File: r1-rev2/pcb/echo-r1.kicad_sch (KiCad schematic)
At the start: 74 parts, among them J2 TYPE-C-31-M-12, J3 TF-115, J6 PM254-1-06-W-8.5, J7 ILI9342C, Q4 AO3401A, SW1 POWER, SW10 DPAD→, SW11 START, SW12 SELECT, SW13 VOL+, SW14 VOL-, SW2 HOLD, SW3 A, SW4 B, SW5 X, SW6 Y, SW7 DPAD↑, SW8 DPAD↓, SW9 DPAD←, U7 STM32H7R3Z8Jx, U8 W958D8NBYA5I, Y1 SC-32S32.768kHz20PPM12.5pF, Y2 XTM32024000JT00351001

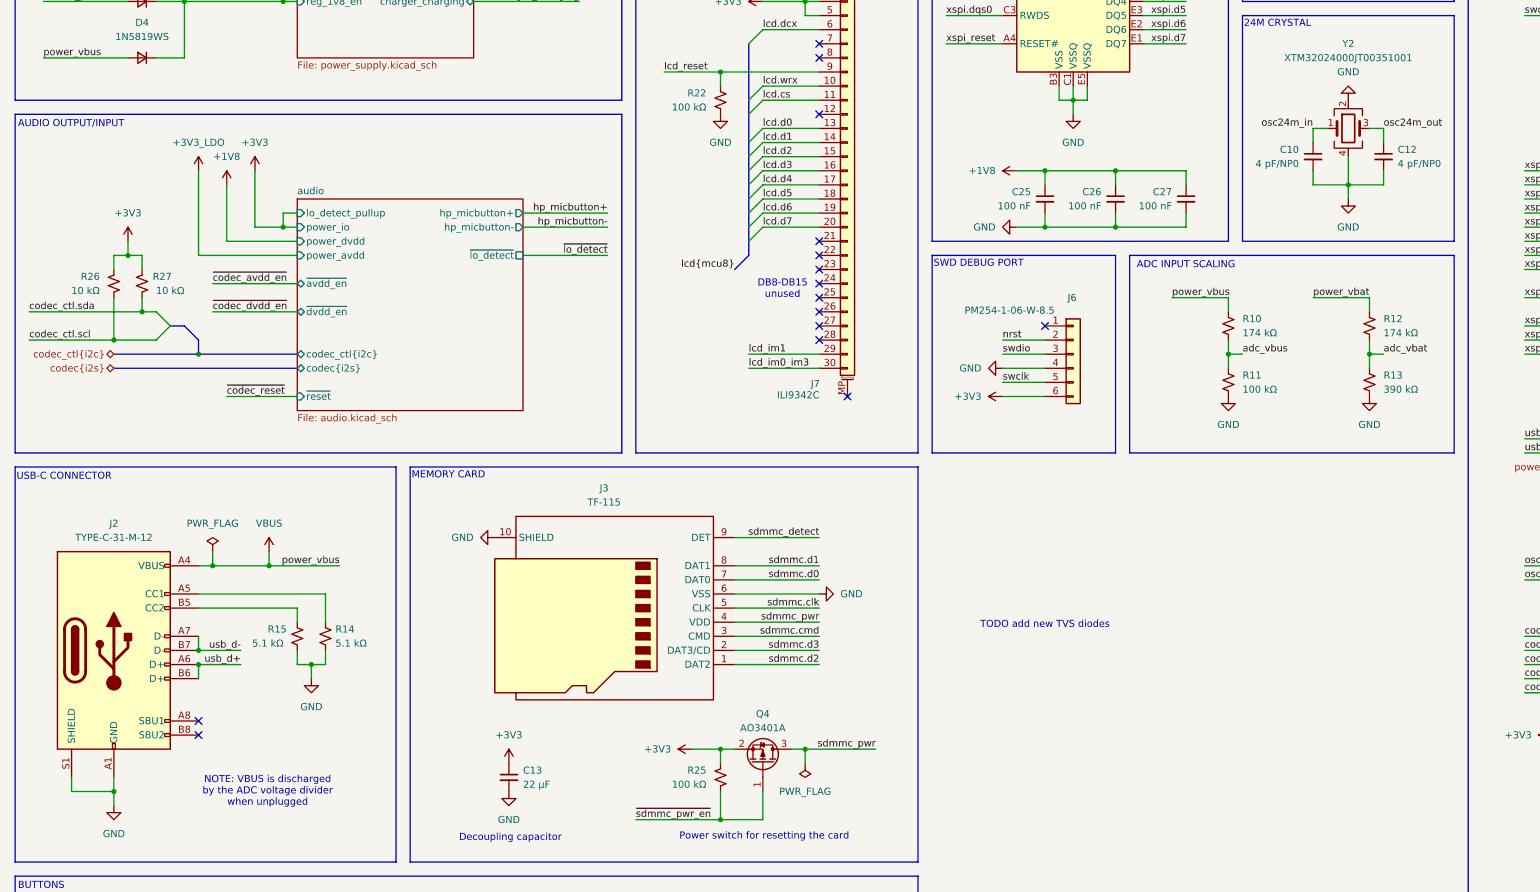
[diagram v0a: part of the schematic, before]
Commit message: R1-Rev2: optimize resistor values
- Resistors used for the ADC dividers were way too high; I didn't
  take into account how the RC constant affected ADC performance
  so the conversion accuracy was probably poor. The new values are
  based on ST's recommendations and the theoretical resolution is
  computed in a spreadsheet.
- Simplify LO detect, originally I had the idea of a "wake on jack
  insert" feature but this is not possible for the headphone jack
  because it is only polled over I2C. The reason for the big 1M
  resistor that was there in Rev1 was to keep the effect on ground
  minimal. If the MCU is powered up then a simple hi-z input with
  internal pullup does the job better.
- Standardize on just 4 unique resistor values to reduce the cost
  of assembly: 5.1k is needed for USB, 2.2k for micbias and battery
  charge reference, and 15k and 68k for voltage reference. Other
  resistors have been rounded to one of these.
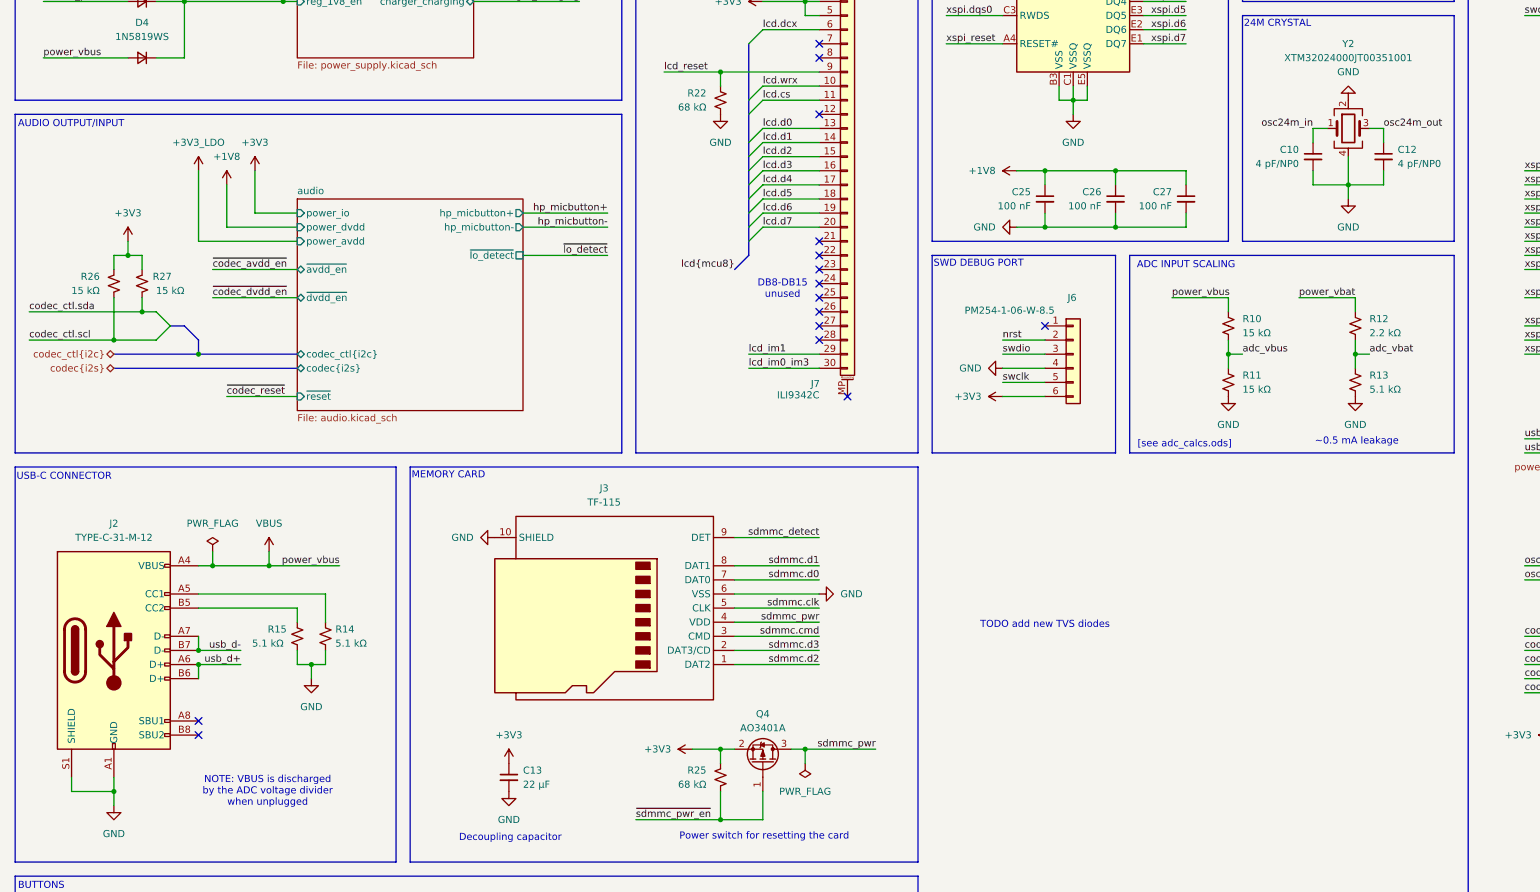
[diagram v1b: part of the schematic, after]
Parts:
- R10: value 174 kΩ -> 15 kΩ
- R11: value 100 kΩ -> 15 kΩ
- R12: value 174 kΩ -> 2.2 kΩ
- R13: value 390 kΩ -> 5.1 kΩ
- R22, R25: value 100 kΩ -> 68 kΩ
- R26, R27: value 10 kΩ -> 15 kΩ
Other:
- sheet audio ports: added none; removed lo_detect_pullup
- note added: "[see adc_calcs.ods]"
- note added: "~0.5 mA leakage"
- moved on the sheet: R12, R13

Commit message: R1-Rev2: strip LCSC part numbers from schematic
These will be managed in a separate BOM spreadsheet going forward.
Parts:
- C10, C12: LCSC# C541337 -> (none)
- C11, C9: LCSC# C161328 -> (none)
- C13: LCSC# C91606 -> (none)
- C25, C26, C27, C28, C29, C30, C31, C32, C33, C34, C35, C36, C37, C38, C39, C40, C41, C42, C43, C44, C45, C46, C47, C48, C49, C50, C51, C52, C53, C54, C55: LCSC# C77020 -> (none)
- D1, D2, D3, D4: LCSC# C191023 -> (none)
- J2: LCSC# C165948 -> (none)
- J3: LCSC# C720505 -> (none)
- J6: LCSC# C2897388 -> (none)
- Q4: LCSC# C347476 -> (none)
- R10, R12: LCSC# C2933159 -> (none)
- R11, R22, R25: LCSC# C60491 -> (none)
- R13: LCSC# C23150 -> (none)
- R14, R15: LCSC# C25905 -> (none)
- R26, R27: LCSC# C60490 -> (none)
- SW1, SW13, SW14: LCSC# C318941 -> (none)
- SW11, SW12: LCSC# C720477 -> (none)
- SW2: LCSC# C431541 -> (none)
- Y1: LCSC# C97606 -> (none)
- Y2: LCSC# C37635376 -> (none)

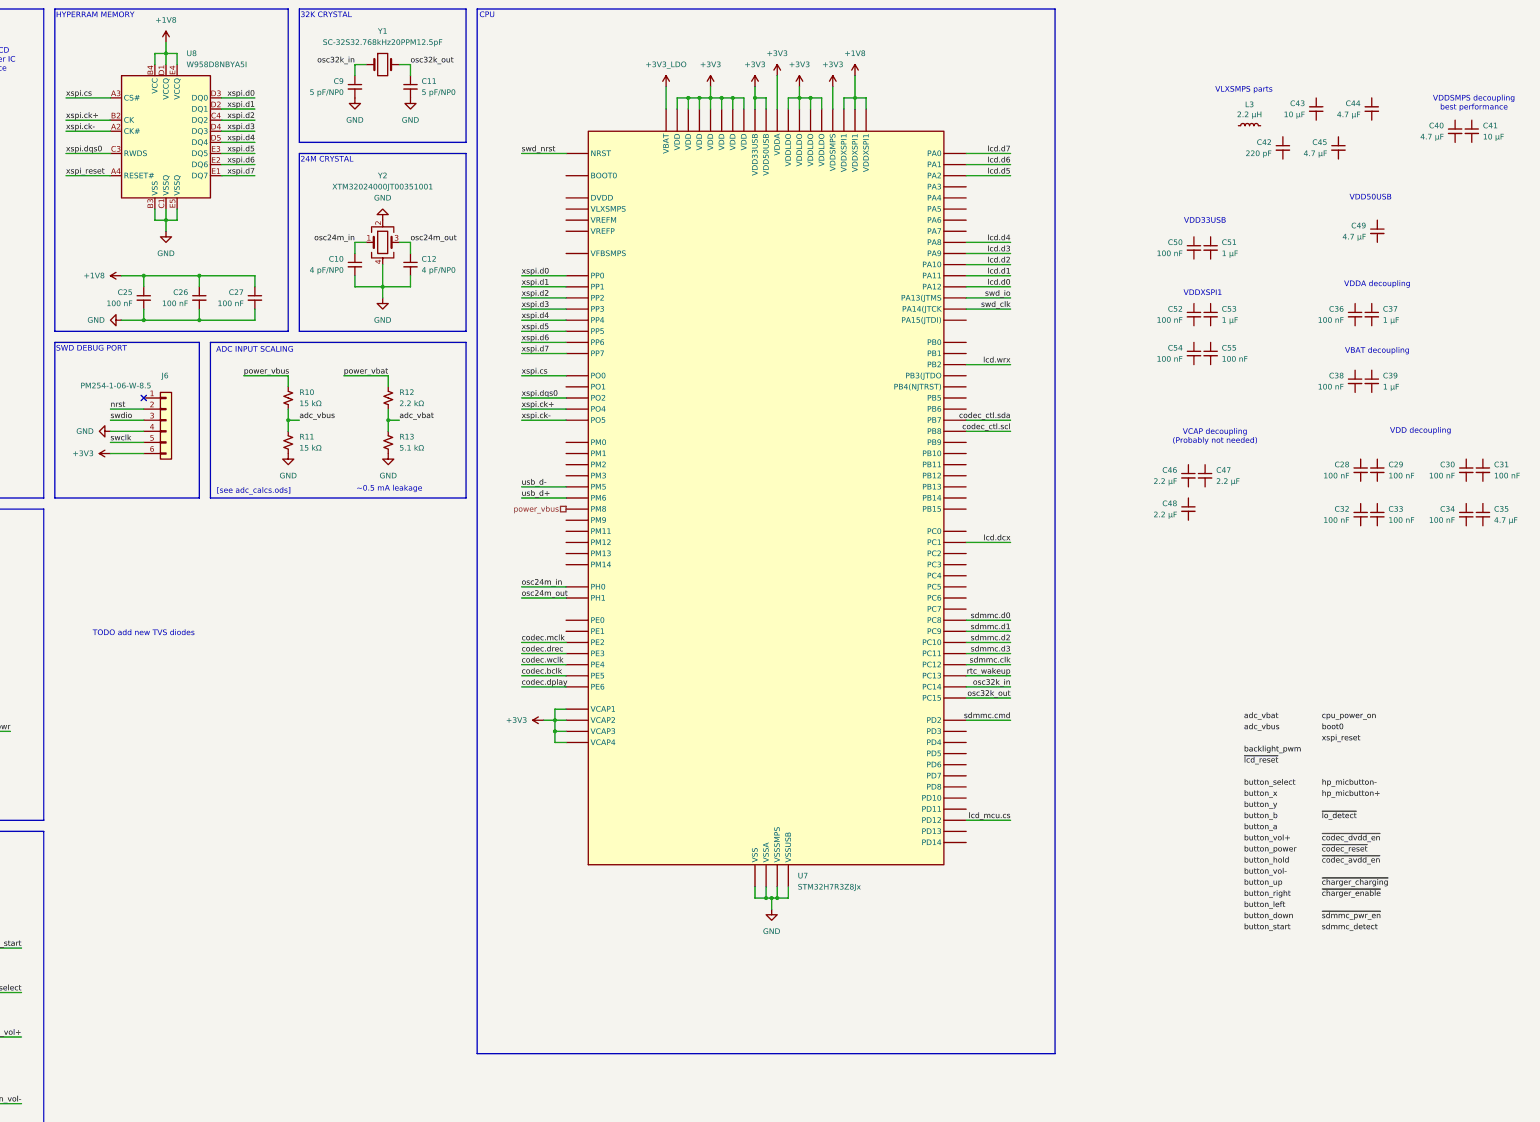
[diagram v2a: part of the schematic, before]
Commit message: R1-Rev2: connect decoupling caps on STM32
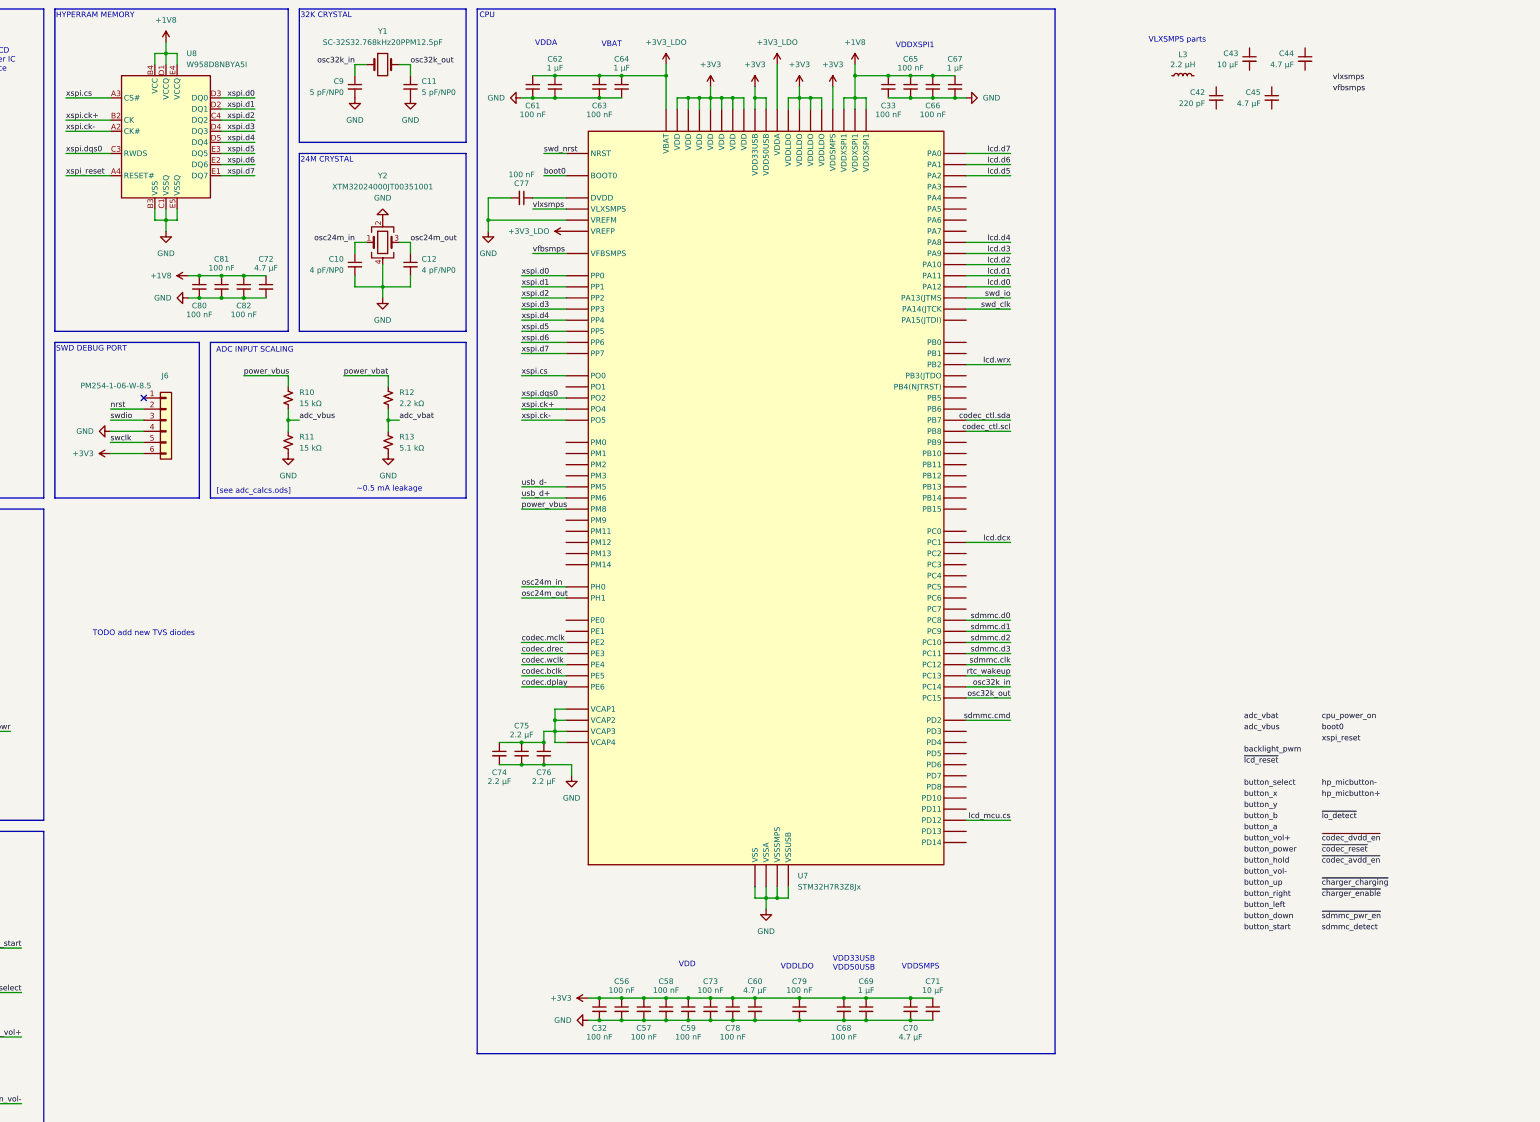
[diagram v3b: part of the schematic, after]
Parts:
- removed C25, C26, C27, C28, C29, C30, C31, C34, C36, C38, C50, C52, C54, C55: 100 nF, Capacitor_SMD:C_0402_1005Metric, symbol Device:C_Small
- removed C35, C40, C49: 4.7 µF, Capacitor_SMD:C_0402_1005Metric, symbol Device:C_Small
- removed C37, C39, C51, C53: 1 µF, Capacitor_SMD:C_0402_1005Metric, symbol Device:C_Small
- removed C41: 10 µF, Capacitor_SMD:C_0402_1005Metric, symbol Device:C_Small
- removed C46, C47, C48: 2.2 µF, Capacitor_SMD:C_0402_1005Metric, symbol Device:C_Small
- added C56, C57, C58, C59, C61, C63, C65, C66, C68, C73, C77, C78, C79, C80, C81, C82: 100 nF, Capacitor_SMD:C_0402_1005Metric, symbol Device:C_Small
- added C60, C70, C72: 4.7 µF, Capacitor_SMD:C_0402_1005Metric, symbol Device:C_Small
- added C62, C64, C67, C69: 1 µF, Capacitor_SMD:C_0402_1005Metric, symbol Device:C_Small
- added C71: 10 µF, Capacitor_SMD:C_0402_1005Metric, symbol Device:C_Small
- added C74, C75, C76: 2.2 µF, Capacitor_SMD:C_0402_1005Metric, symbol Device:C_Small
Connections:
- net +1V8: now also C33.1, C65.1, C66.1, C67.1, C72.1, C80.1, C81.1, C82.1
- net +3V3: now also C32.1, C56.1, C57.1, C58.1, C59.1, C60.1, C68.1, C69.1, C70.1, C71.1, C73.1, C78.1, C79.1; no longer U7.E5 (VCAP4), U7.F8 (VCAP3), U7.H6 (VCAP1), U7.H8 (VCAP2), U7.J3 (VDDA)
- net +3V3_LDO: now also U7.J3 (VDDA), U7.K3 (VREFP), C61.1, C62.1, C63.1, C64.1
- net GND: now also C32.2, C33.2, U7.H5 (VREFM), C56.2, C57.2, C58.2, C59.2, C60.2, C61.2, C62.2, C63.2, C64.2, C65.2, C66.2, C67.2, C68.2, C69.2, C70.2, C71.2, C72.2, C73.2, C74.2, C75.2, C76.2, C77.2, C78.2, C79.2, C80.2, C81.2, C82.2
- net boot0: now also U7.A6 (BOOT0)
- net at U7.C8 (DVDD): now also C77.1
- net vlxsmps: now reaches U7.F1 (VLXSMPS)
- net vfbsmps: now reaches U7.F3 (VFBSMPS)
- new net: C74.1, C75.1, C76.1, U7.E5 (VCAP4), U7.F8 (VCAP3), U7.H6 (VCAP1), U7.H8 (VCAP2)
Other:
- note added: "VBAT"
- note added: "VDD"
- note added: "VDD33USB VDD50USB"
- note added: "VDDA"
- note added: "VDDLDO"
- note added: "VDDSMPS"
- note removed: "VBAT decoupling"
- note removed: "VCAP decoupling (Probably not needed)"
- note removed: "VDD decoupling"
- note removed: "VDD33USB"
- note removed: "VDD50USB"
- note removed: "VDDA decoupling"
- note removed: "VDDSMPS decoupling best performance"
- moved on the sheet: C32, C42, C43, C44, C45, L3
